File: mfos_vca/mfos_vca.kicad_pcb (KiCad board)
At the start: 2 copper layers, 49.5 x 106.5 mm, 69 parts, among them J1 CV A, J2 Signal In A, J3 Signal Out A, J4 CV B, J5 Signal In B, J6 Signal Out B, J7 Conn_02x05_Odd_Even, Q1 2N3904, Q2 2N3906, Q3 2N3904, Q4 2N3906, SW1 SW_SPDT, SW2 SW_SPDT, U1 TL074, U2 LM13700

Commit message: update vca pcb with schematic fixes
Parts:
- added R13: 100k, Resistor_THT:R_Axial_DIN0207_L6.3mm_D2.5mm_P10.16mm_Horizontal, F.Cu at (134.8, 84.5)
- added R32: 100k, Resistor_THT:R_Axial_DIN0207_L6.3mm_D2.5mm_P10.16mm_Horizontal, F.Cu at (123.5, 92.7)
- R19: renamed from R18; moved to B.Cu
- moved RV4 6.93 mm to (123.5, 97.5)
- moved J4 6.63 mm to (123.5, 108.0)
- moved J5 6.47 mm to (123.5, 118.0)
- moved R28 5.35 mm to (123.5, 136.5)
- moved C3 4.88 mm to (123.5, 140.5)
- moved C4 4.38 mm to (123.5, 145.5)
- moved RV3 1.65 mm to (142.1, 79.5)
- renumbered R13 to R14, R14 to R15, R15 to R16, R16 to R17, R17 to R18, R19 to R20, R20 to R21, R21 to R22, R22 to R23, R23 to R24, R24 to R25, R25 to R26, R26 to R27, R27 to R28, R28 to R29, R29 to R30, R30 to R31, R31 to R33, R32 to R34, R33 to R35, R34 to R36, R35 to R37, R36 to R38, R37 to R39, R38 to R40
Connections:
- R10 pad 2: Net-(U1D-+) -> Net-(U1D--)
- R11 pad 2: Net-(U1D--) -> Net-(U1D-+)
- R14 pad 1: Net-(U1D--) -> Net-(U1D-+)
- R20 pad 2: Net-(U1B-+) -> Net-(U1B--)
- R21 pad 2: Net-(U1B-+) -> Net-(U1B--)
- R22 pad 2: Net-(U1B--) -> Net-(U1B-+)
- R23 pad 2: Net-(U2A--) -> Net-(U2A-+)
- R24 pad 2: Net-(R23-Pad2) -> Net-(R24-Pad2)
- R25 pad 1: Net-(U1B--) -> Net-(U1B-+)
- R26 pad 1: Net-(U1B-+) -> Net-(U1B--)
- R29 pad 2: Net-(U1A-+) -> Net-(U1A--)
- R30 pad 2: Net-(U1A--) -> Net-(U1A-+)
- R31 pad 2: Net-(R23-Pad2) -> Net-(R24-Pad2)
- R33 pad 1: Net-(U1A--) -> Net-(U1A-+)
- R35 pad 1: Net-(R23-Pad2) -> Net-(R24-Pad2)
- RV6 pad 1: Net-(U2A--) -> Net-(U2A-+)
- RV6 pad 2: Net-(U2A--) -> Net-(U2A-+)
- U2 pad 10: Net-(R23-Pad2) -> Net-(R24-Pad2)
- U2 pad 12: Net-(SW2-B) -> Net-(R24-Pad2)
- U2 pad 13: Net-(U2A--) -> GND
- U2 pad 14: GND -> Net-(U2A-+)
- U2 pad 16: Net-(R23-Pad2) -> Net-(SW2-B)
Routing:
- net Net-(R23-Pad2): track 97.1 -> 0.00 mm, vias 1 -> 0
- net Net-(R24-Pad2): track 0.00 -> 82.2 mm, vias 0 -> 2
- net Net-(U2A-+): track 0.00 -> 39.8 mm, vias 0 -> 1
- net GND: track 44.3 -> 9.33 mm, vias 2 -> 1
- net Net-(U2A--): track 34.6 -> 0.00 mm, vias 3 -> 0
- net Net-(SW2-B): track 32.8 -> 15.7 mm, vias 1 -> 0
- net +12V: track 256.7 -> 270.2 mm
- net Net-(U1A-+): track 33.1 -> 45.0 mm, vias 0 -> 1
- net Net-(U1B-+): track 44.5 -> 33.5 mm
- net Net-(R32-Pad2): track 51.0 -> 60.6 mm, vias 1 -> 2
- net Net-(U1B--): track 32.2 -> 41.7 mm
- net Net-(R21-Pad1): track 31.1 -> 22.3 mm, vias 2 -> 0
- net Net-(U1A--): track 47.2 -> 39.8 mm
- net -12V: track 286.4 -> 293.6 mm
- net Net-(J4-PadT): track 13.3 -> 6.89 mm
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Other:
- board text added: "LM13700 VCA (v1.1) Jesse Holzman"
- board text removed: "LM13700 VCA Jesse Holzman"

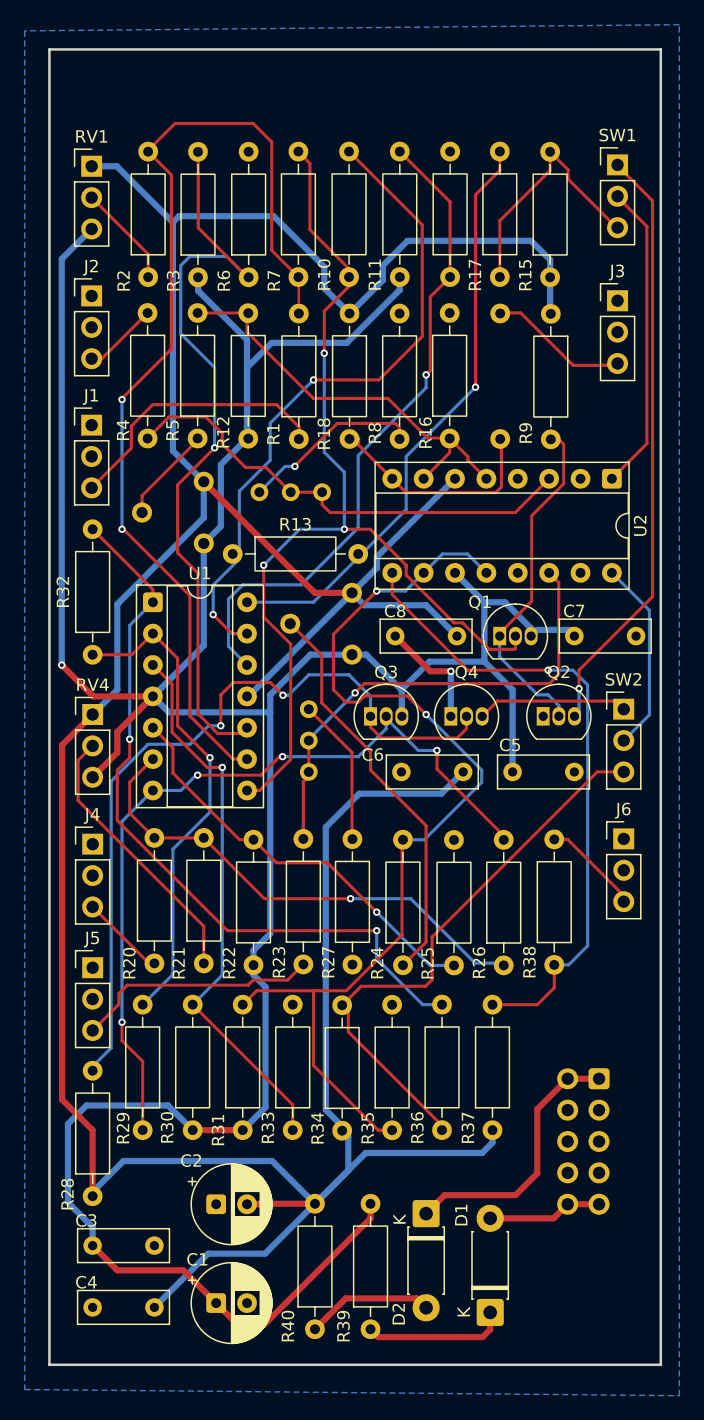
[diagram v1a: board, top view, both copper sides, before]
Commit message: fix pcb holes
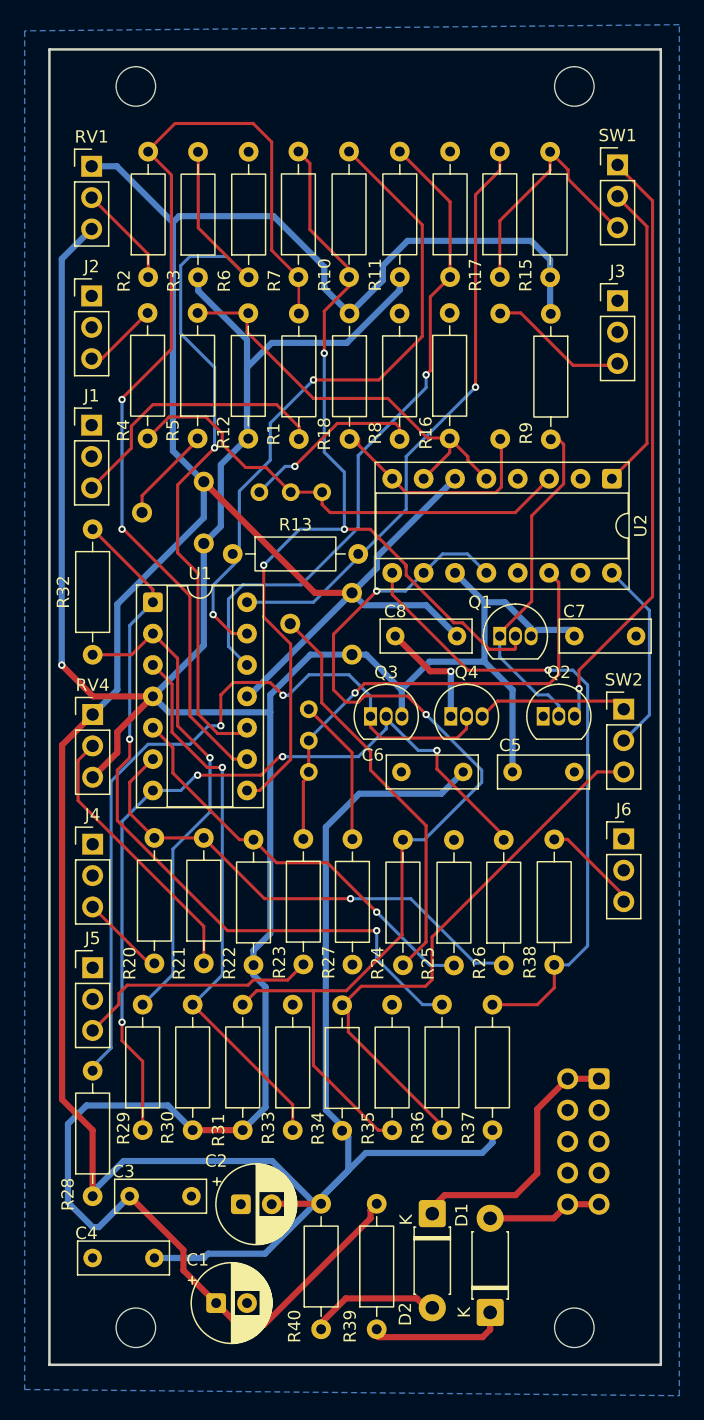
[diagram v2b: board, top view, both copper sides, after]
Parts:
- added REF**: MountingHole_3.2mm_M3, MountingHole:MountingHole_3.2mm_M3, F.Cu at (127.0, 46.6)
- added REF**: MountingHole_3.2mm_M3, MountingHole:MountingHole_3.2mm_M3, F.Cu at (162.5, 147.2)
- added REF**: MountingHole_3.2mm_M3, MountingHole:MountingHole_3.2mm_M3, F.Cu at (127.0, 147.2)
- added REF**: MountingHole_3.2mm_M3, MountingHole:MountingHole_3.2mm_M3, F.Cu at (162.5, 46.6)
- moved C3 5.00 mm to (126.5, 136.5)
- moved C4 4.00 mm to (123.5, 141.5)
- moved C2 2.00 mm to (135.5, 137.2)
- moved D2 0.50 mm to (151.0, 137.9)
- moved R39 0.50 mm to (146.5, 147.3)
- moved R40 0.50 mm to (142.0, 147.3)
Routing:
- net -12V: track 293.6 -> 290.0 mm
- net +12V: track 270.2 -> 272.6 mm
